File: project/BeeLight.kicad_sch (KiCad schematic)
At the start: 23 parts, among them IC101 BT40F, IC102 APDS-9306-065, IC103 BME688, Q101 BSS84, SW101 JOIN, X102 DEBUG

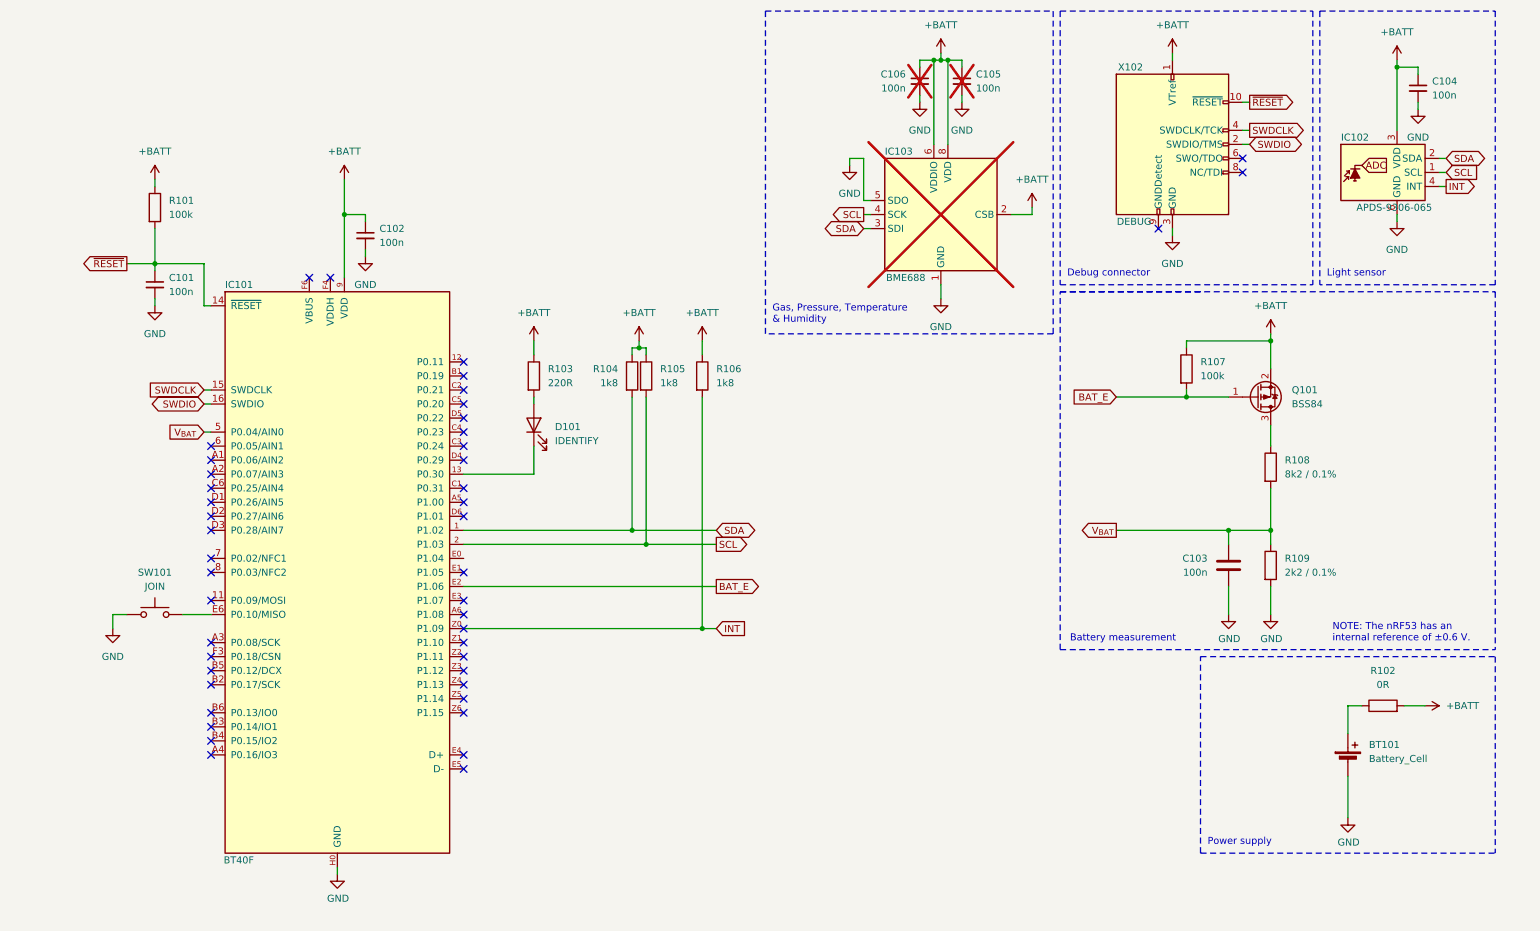
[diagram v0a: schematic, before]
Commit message: Replace nRF53 with nRF54L
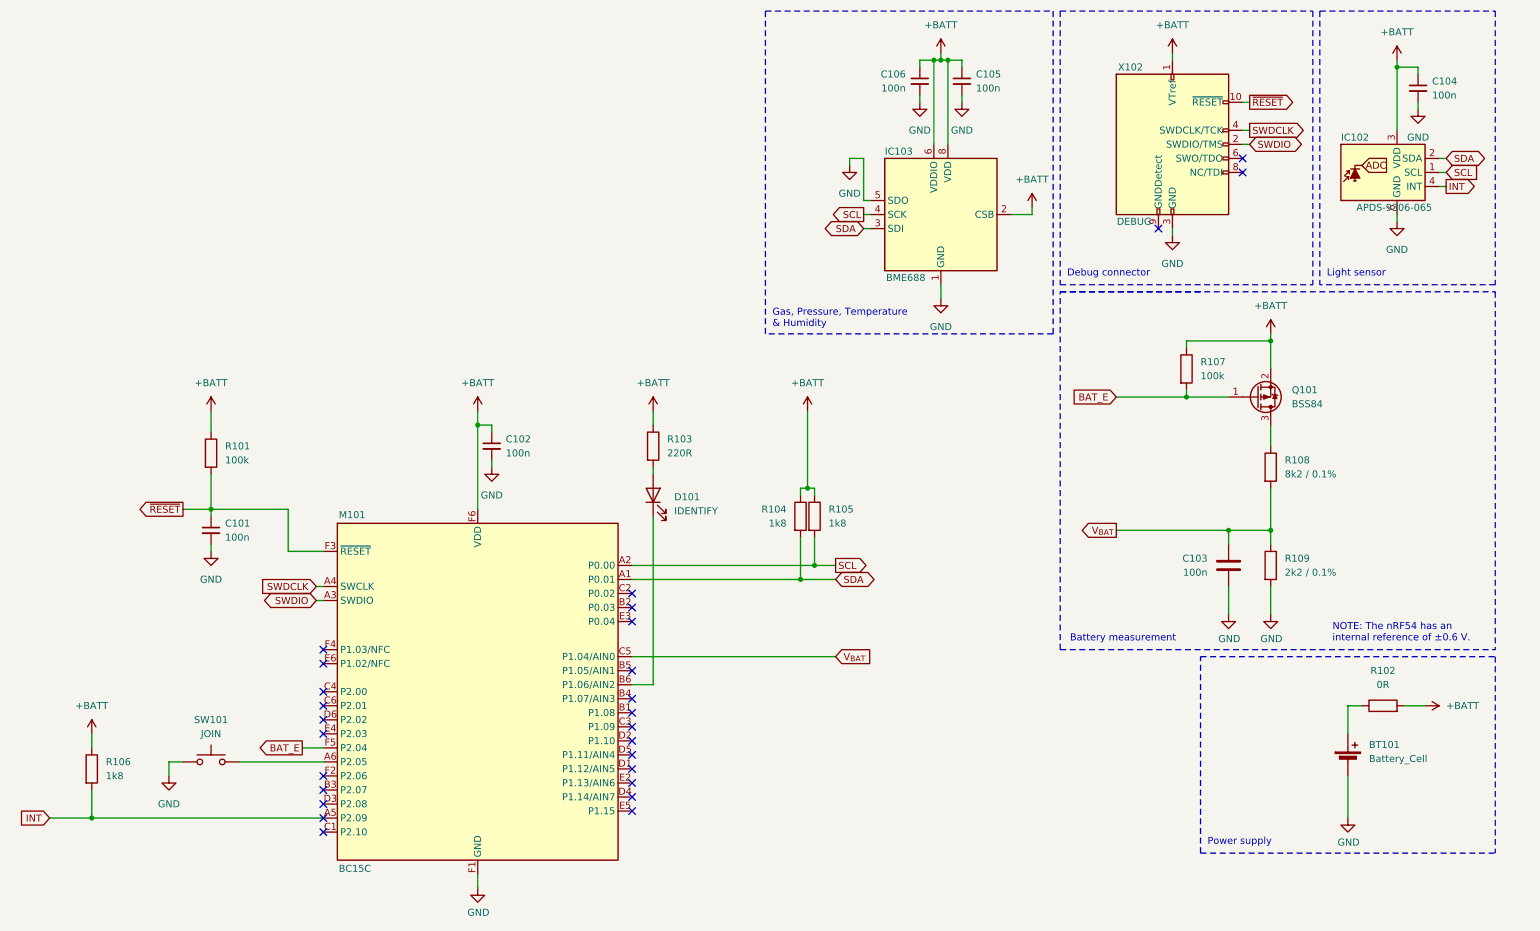
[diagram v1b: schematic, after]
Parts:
- removed IC101: BT40F, Fanstel:XCVR_BT40F, symbol Fanstel:BT40F
- added M101: BC15C, Fanstel:BC15C, symbol Fanstel:BC15C
- C105, C106, IC103: now fitted; now in the parts list
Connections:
- net +BATT: now also M101.F6 (VDD)
- net BAT_E: now also M101.F5 (P2.04)
- net GND: now also M101.E1 (GND), M101.F1 (GND)
- net INT: now also M101.A5 (P2.09)
- net SCL: now also M101.A2 (P0.00)
- net SDA: now also M101.A1 (P0.01)
- net SWDCLK: now also M101.A4 (SWCLK)
- net SWDIO: now also M101.A3 (SWDIO)
- net V_{BAT}: now also M101.C5 (P1.04/AIN0)
- net ~{RESET}: now also M101.F3 (~{RESET})
- net at D101.1 (K): now also M101.B6 (P1.06/AIN2)
- net at SW101.2: now also M101.A6 (P2.05)
- no-connect marks 46 -> 27
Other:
- note added: "NOTE: The nRF54 has an internal reference of ±0.6 V."
- note removed: "NOTE: The nRF53 has an internal reference of ±0.6 V."
- moved on the sheet: C101, C102, D101, R101, R103, R104, R105, R106, SW101
